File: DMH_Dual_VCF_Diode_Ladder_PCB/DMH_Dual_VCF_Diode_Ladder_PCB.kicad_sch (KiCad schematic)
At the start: 0 parts

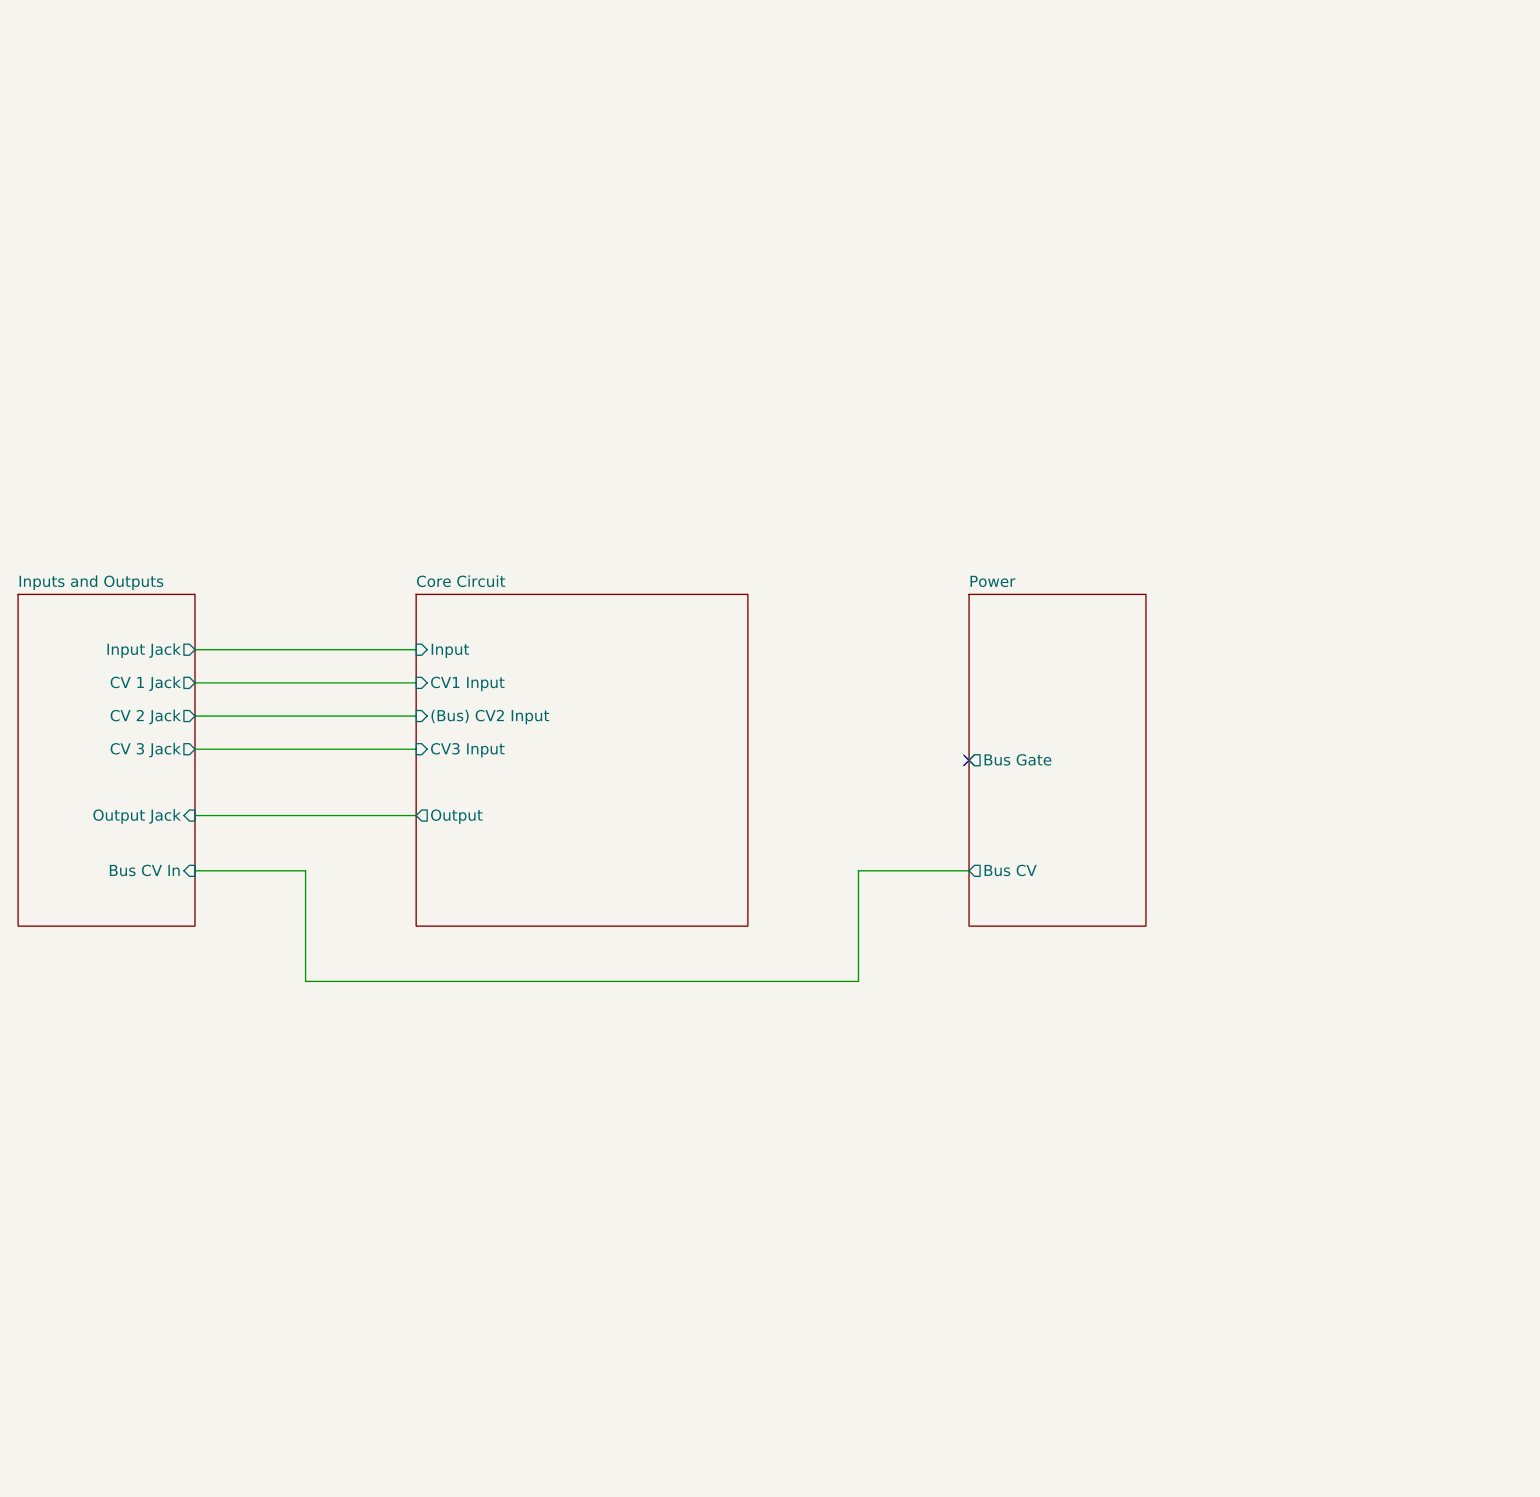
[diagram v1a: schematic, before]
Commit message: Started circuit schematic
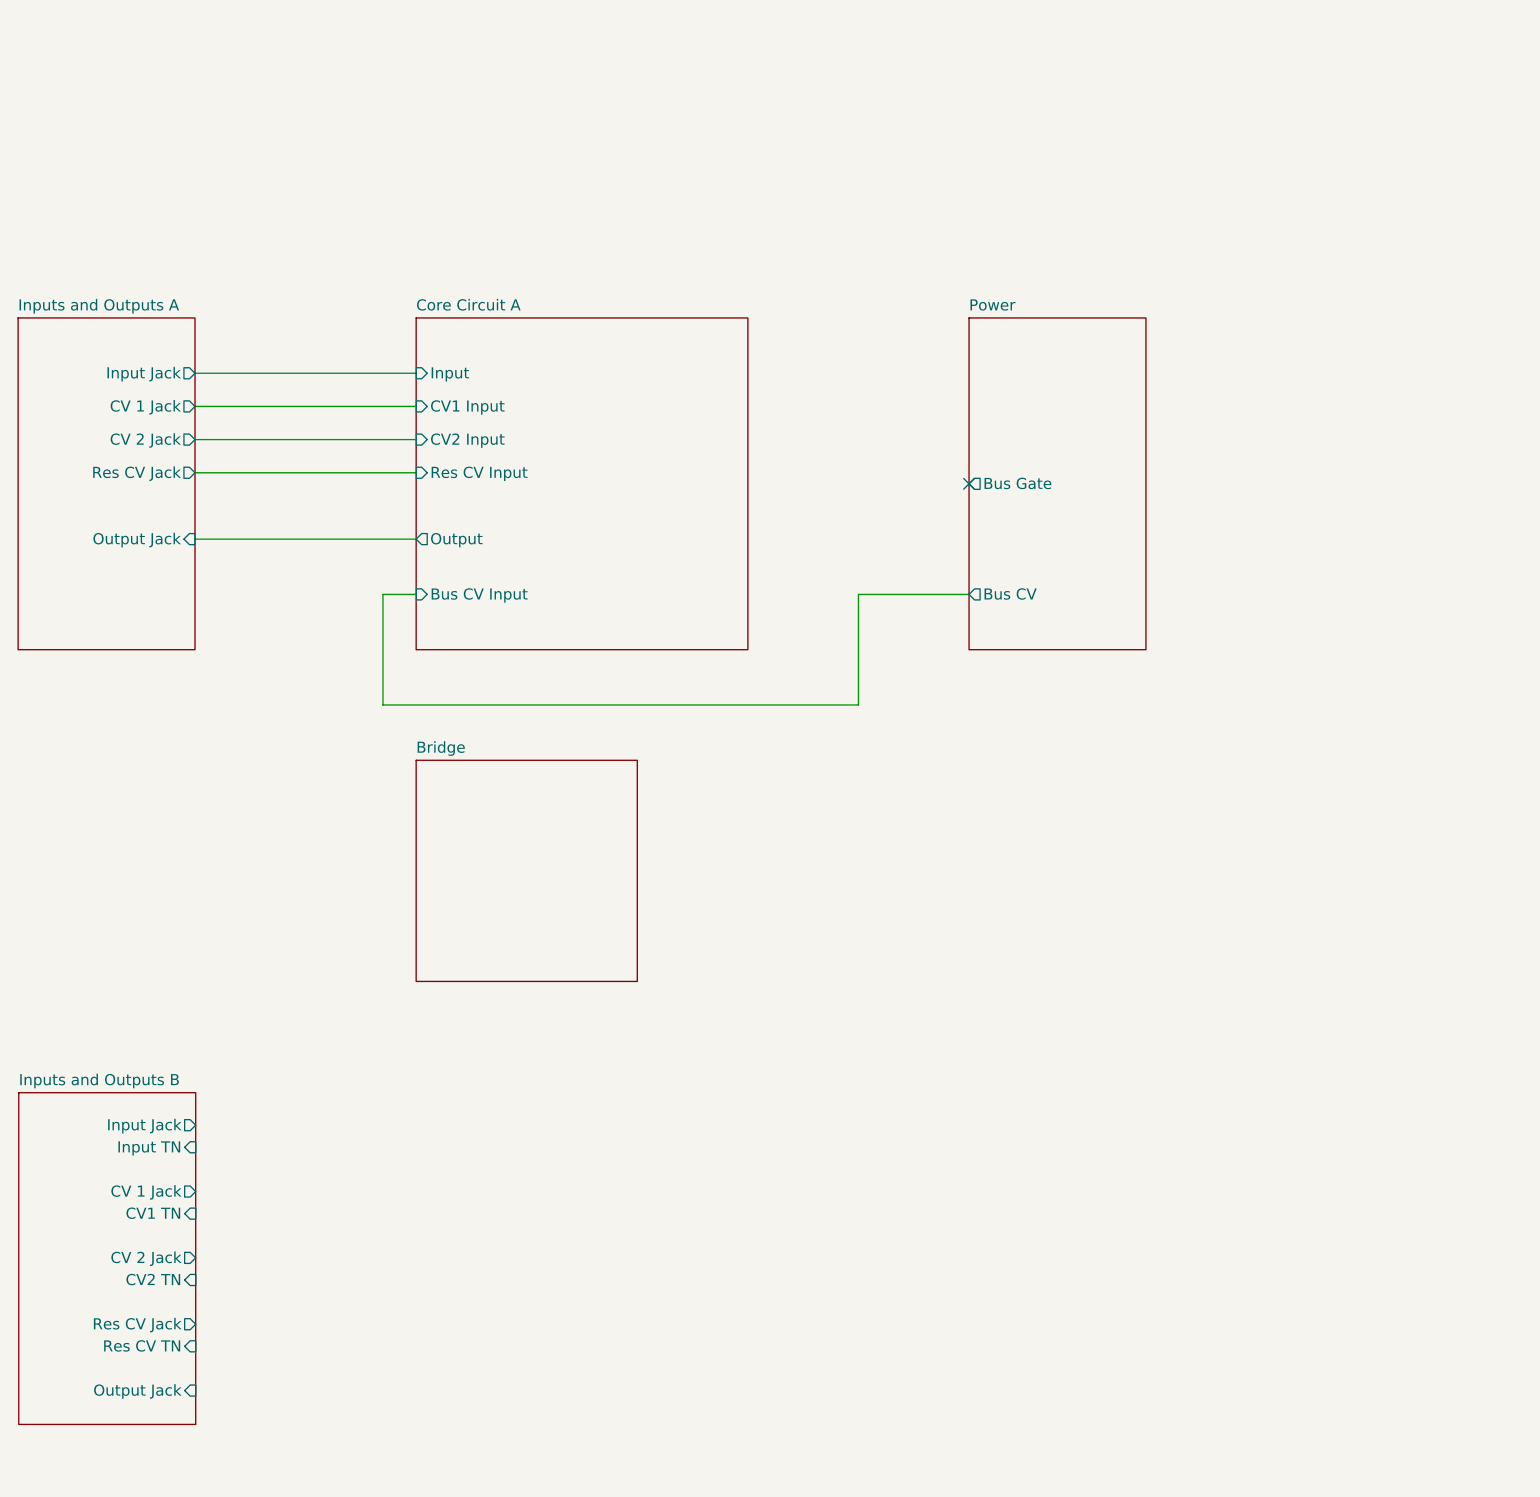
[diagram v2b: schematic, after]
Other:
- sheet Core Circuit renamed Core Circuit A
- sheet Inputs and Outputs renamed Inputs and Outputs A
- added sheet Bridge (Bridge.kicad_sch)
- added sheet Inputs and Outputs B (Inputs_and_Outputs_B.kicad_sch)
- sheet Core Circuit A: file Core_Circuit.kicad_sch -> Core_Circuit_A.kicad_sch
- sheet Core Circuit A ports: added Bus CV Input, CV2 Input, Res CV Input; removed (Bus) CV2 Input, CV3 Input
- sheet Inputs and Outputs A: file Inputs_and_Outputs.kicad_sch -> Inputs_and_Outputs_A.kicad_sch
- sheet Inputs and Outputs A ports: added Res CV Jack; removed Bus CV In, CV 3 Jack

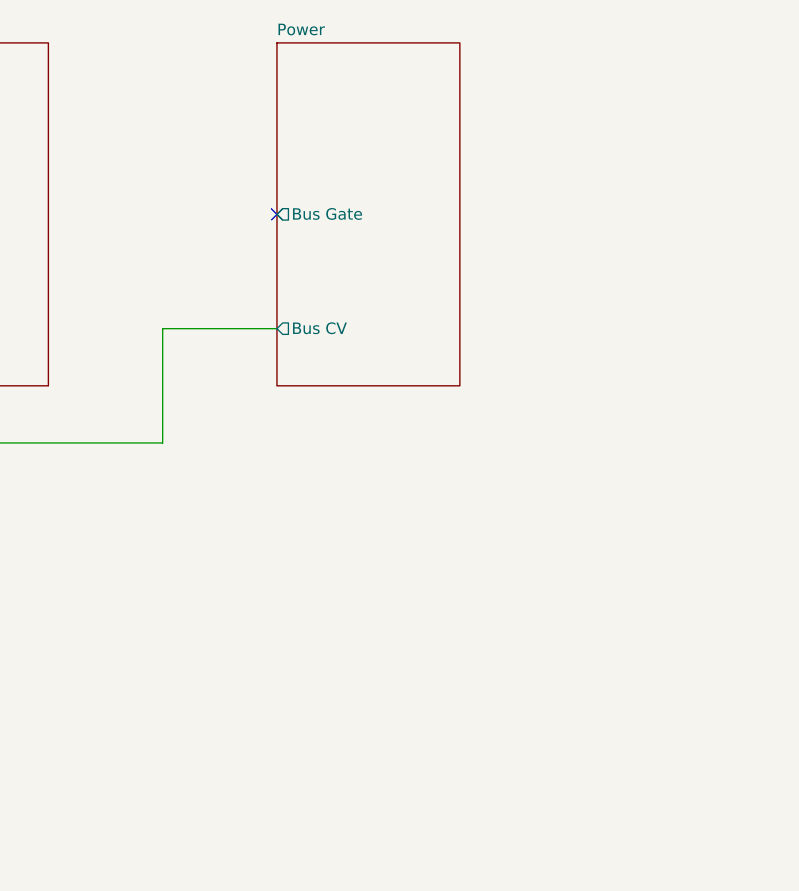
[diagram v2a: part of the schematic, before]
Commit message: Starting Res CV design
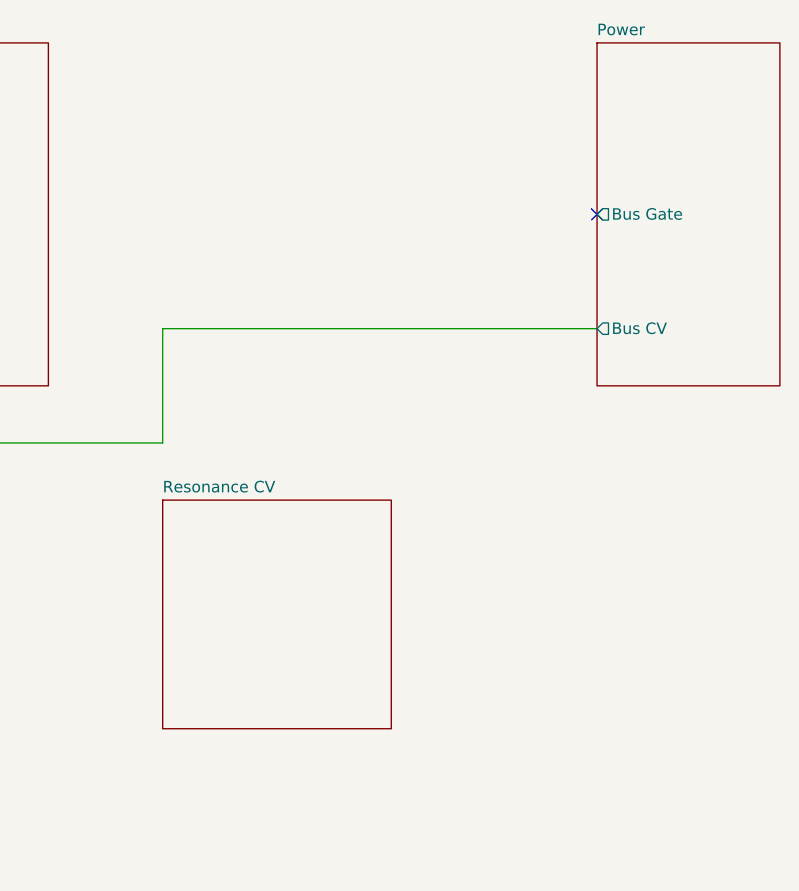
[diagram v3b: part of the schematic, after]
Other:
- added sheet Resonance CV (Resonance_CV.kicad_sch)
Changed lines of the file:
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@@
 	)
 	(no_connect
-		(at 127 69.85)
-	)
-	(wire
-		(pts
-			(xy 114.3 82.55) (xy 127 82.55)
+		(at 162.56 69.85)
+	)
+	(wire
+		(pts
+			(xy 114.3 82.55) (xy 162.56 82.55)
 		)
 		(stroke
@@
 	)
 	(sheet
-		(at 127 50.8)
+		(at 162.56 50.8)
 		(size 20.32 38.1)
 		(fields_autoplaced yes)
@@
 		)
 		(property "Sheetname" "Power"
-			(at 127 50.0884 0)
+			(at 162.56 50.0884 0)
 			(effects
 				(font
@@
 		)
 		(property "Sheetfile" "Power.kicad_sch"
-			(at 127 89.4846 0)
+			(at 162.56 89.4846 0)
 			(effects
 				(font
@@
 		)
 		(pin "Bus Gate" output
-			(at 127 69.85 180)
+			(at 162.56 69.85 180)
 			(effects
 				(font
@@
 		)
 		(pin "Bus CV" output
-			(at 127 82.55 180)
+			(at 162.56 82.55 180)
 			(effects
 				(font
@@
 				)
 			)
+		)
+	)
+	(sheet
+		(at 114.3 101.6)
+		(size 25.4 25.4)
+		(fields_autoplaced yes)
+		(stroke
+			(width 0.1524)
+			(type solid)
+		)
+		(fill
+			(color 0 0 0 0.0000)
+		)
+		(property "Sheetname" "Resonance CV"
+			(at 114.3 100.8884 0)
+			(effects
+				(font
+					(size 1.27 1.27)
+				)
+				(justify left bottom)
+			)
+		)
+		(property "Sheetfile" "Resonance_CV.kicad_sch"
+			(at 114.3 127.5846 0)
+			(effects
+				(font
+					(size 1.27 1.27)
+				)
+				(justify left top)
+				(hide yes)
+			)
+		)
+		(instances
+			(project "DMH_Dual_VCF_Diode_Ladder_PCB"
+				(path "/58f4306d-5387-4983-bb08-41a2313fd315"
+					(page "7")
+				)
+			)
